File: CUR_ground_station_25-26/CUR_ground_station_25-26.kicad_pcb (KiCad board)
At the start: 4 copper layers, 73.9 x 53.3 mm, 81 parts, among them J1 Conn_01x02, J2 UJ20-C-H-G-SMT-P16-TR, J3 Conn_Coaxial_Small, J4 Conn_01x04_Pin, Q1 NTR4003N, Q2 NTR4003N, SW1 PTS815SJM250SMTRLFS, SW2 PTS815SJM250SMTRLFS, SW3 PTS815SJM250SMTRLFS, SW4 PTS815SJM250SMTRLFS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

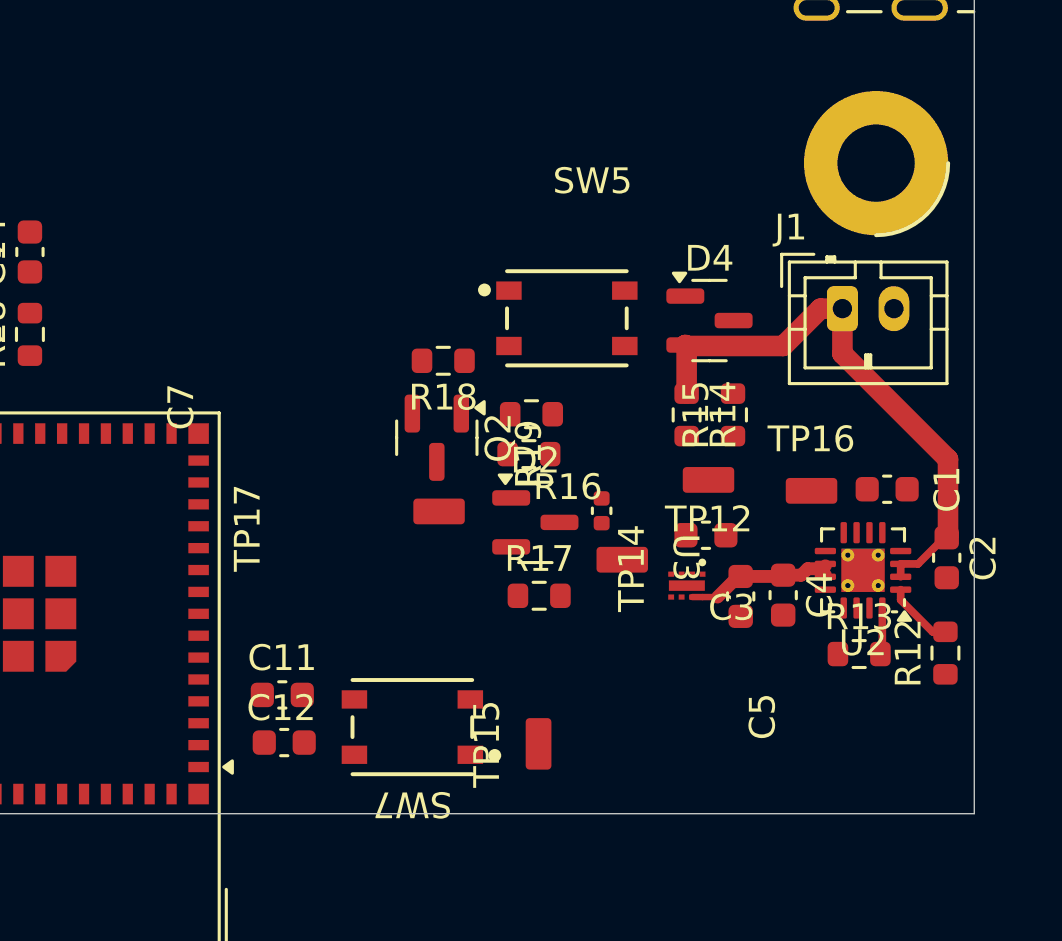
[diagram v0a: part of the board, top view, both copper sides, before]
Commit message: more power layout ing
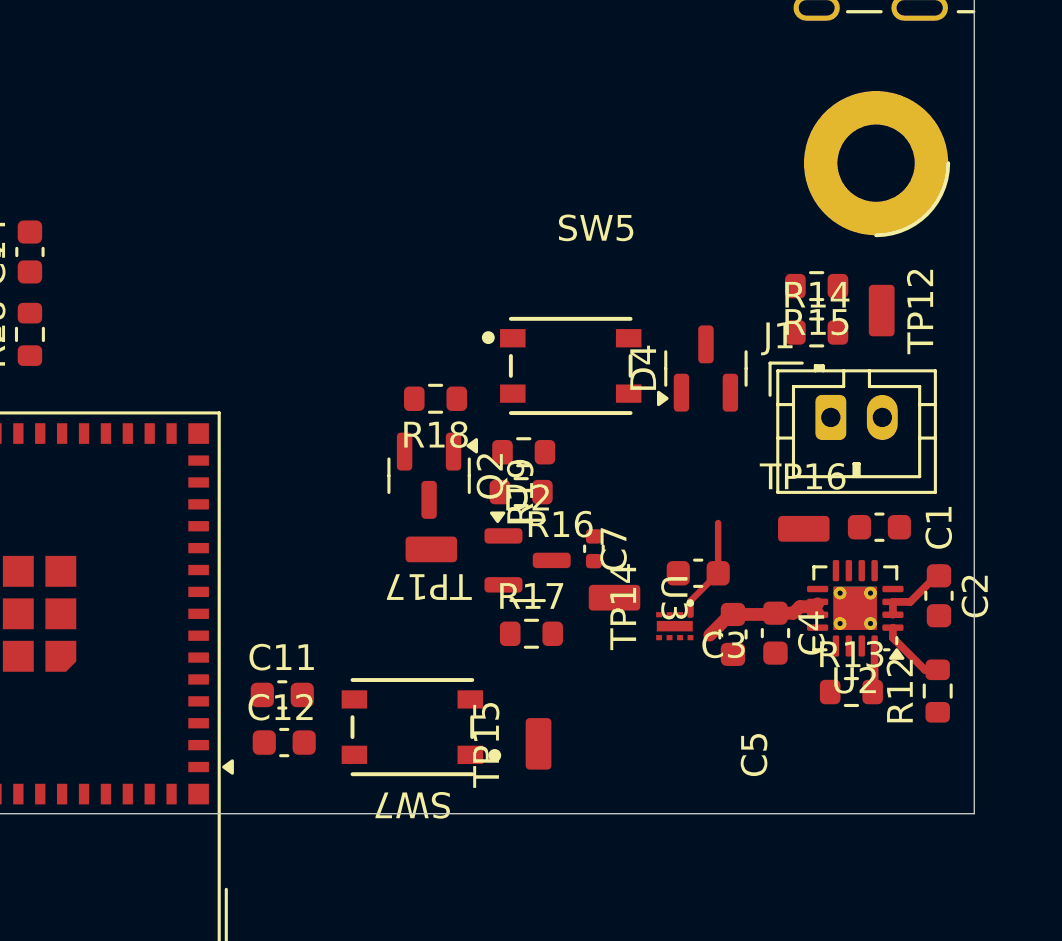
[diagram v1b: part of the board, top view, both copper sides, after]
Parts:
- moved TP12 9.41 mm to (118.8, 83.8), turned to -90 degrees
- moved R14 5.98 mm to (116.3, 84.6), turned to 0 degrees
- moved R15 5.96 mm to (116.3, 82.8), turned to 180 degrees
- moved J1 4.25 mm to (116.8, 87.9)
- moved D4 1.87 mm to (112.0, 86.0), turned to 90 degrees
- moved SW5 1.86 mm to (106.7, 85.9)
- moved U3 1.64 mm to (110.7, 96.0)
- moved C5 1.51 mm to (111.6, 94.0)
- moved R18 1.51 mm to (101.5, 87.2)
- moved TP17 1.51 mm to (101.3, 93.1)
- moved R12 1.51 mm to (121.0, 98.6)
- moved R17 1.51 mm to (105.2, 96.3)
- moved TP16 1.51 mm to (115.8, 92.2)
- moved TP14 1.51 mm to (108.4, 94.9)
- moved C7 1.51 mm to (107.6, 93.0)
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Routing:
- net +BATT: track 21.9 -> 2.78 mm
- net +3V3: track 0.00 -> 4.01 mm
- net IN: track 5.97 -> 4.98 mm

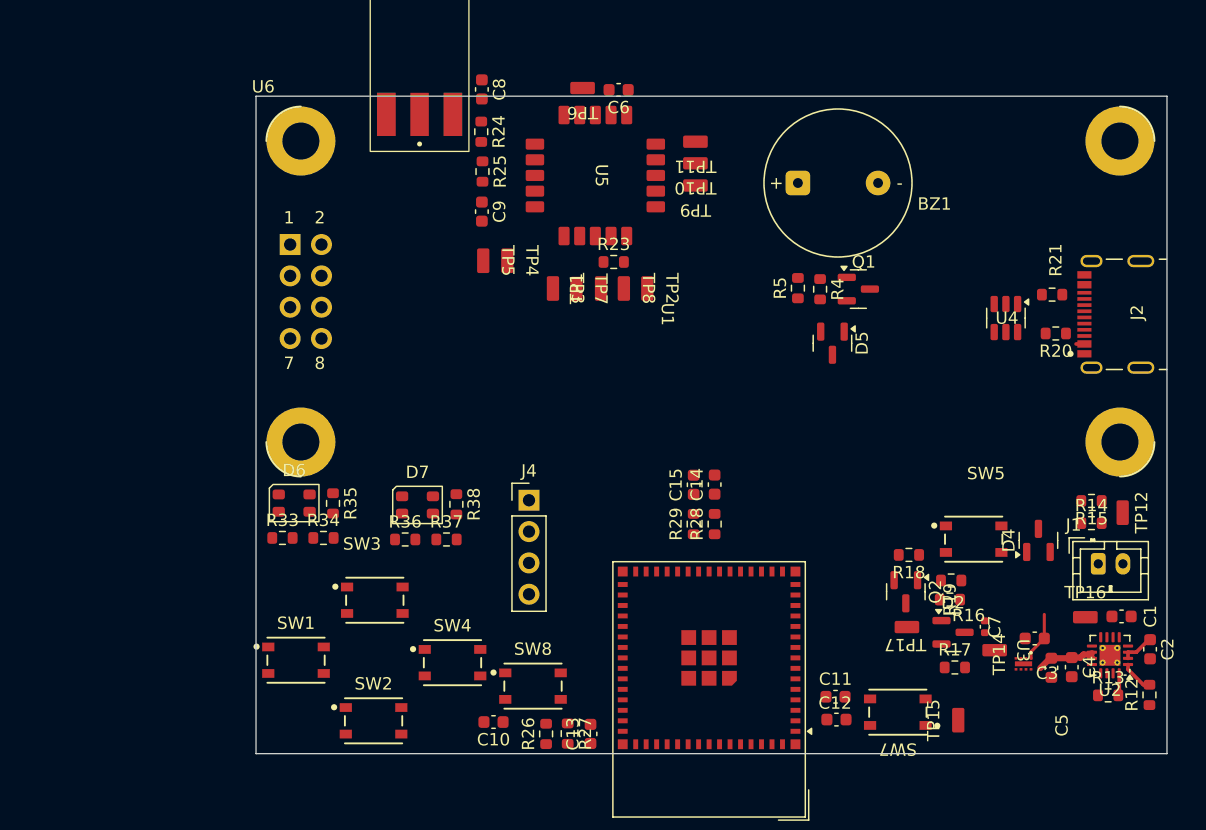
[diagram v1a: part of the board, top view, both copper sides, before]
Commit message: Update board shape, display, and USB C placement
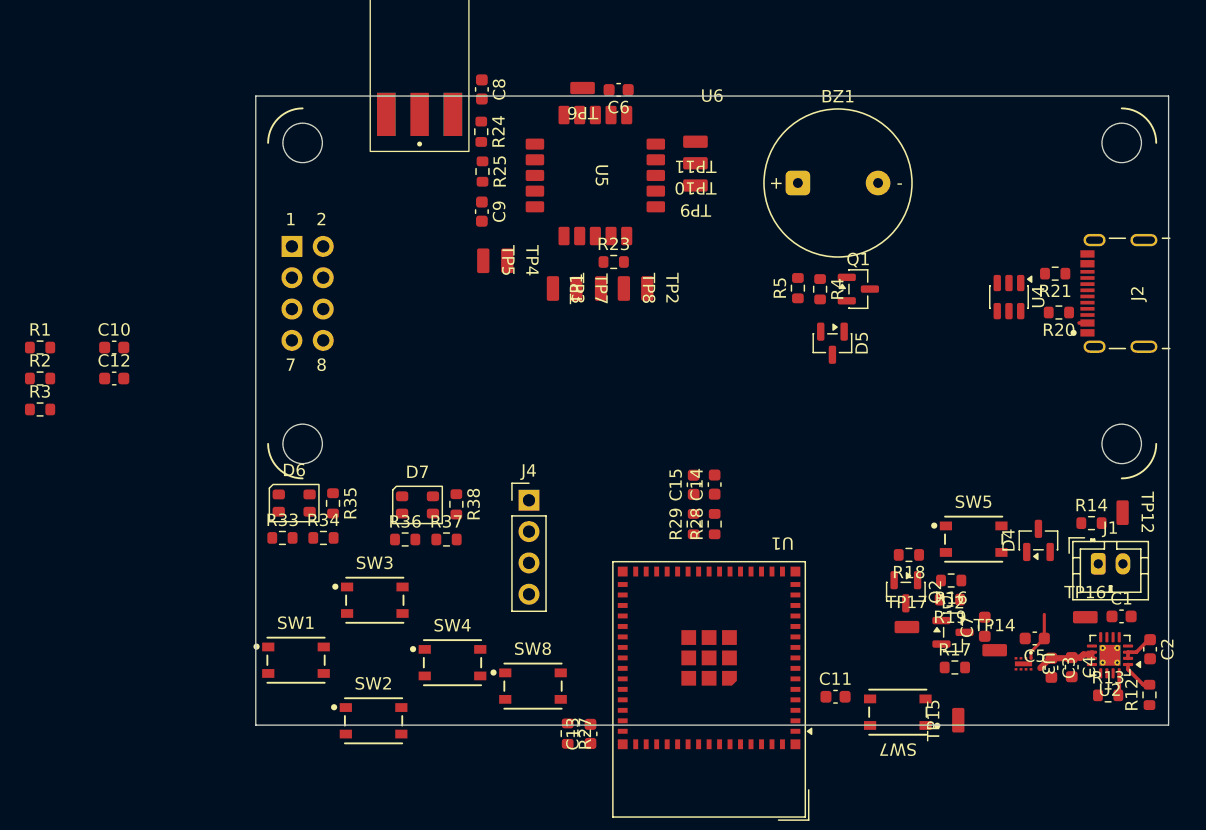
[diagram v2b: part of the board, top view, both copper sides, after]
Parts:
- removed R15: 35k, Resistor_SMD:R_0603_1608Metric
- removed R26: 0, Resistor_SMD:R_0603_1608Metric
- added R1: 10k, Resistor_SMD:R_0603_1608Metric, F.Cu at (31.0, 70.4)
- added R2: 10k, Resistor_SMD:R_0603_1608Metric, F.Cu at (31.0, 72.9)
- added R3: 10k, Resistor_SMD:R_0603_1608Metric, F.Cu at (31.0, 75.4)
- C10: value 100n -> 10u
- C11: value 100n -> 1u
- C12: value 22u -> 10u
- C7: value 1u -> 10u; footprint Capacitor_SMD:C_0402_1005Metric -> Capacitor_SMD:C_0603_1608Metric
- R13: value RC0603FR-071K74L -> 1.74k
- R16, R17: value 300 -> 270
- R18, R19: value 100k -> 10k
- R5: value 150 -> 270
- moved C12 64.8 mm to (37.0, 72.9)
- moved C10 43.2 mm to (37.0, 70.4), turned to 0 degrees
- moved J2 1.72 mm to (120.5, 66.0)
- moved R20 1.72 mm to (113.6, 67.6)
- moved R21 1.72 mm to (113.3, 64.4)
- moved U4 1.72 mm to (109.6, 66.3)
- moved U6 0.21 mm to (49.5, 51.0)
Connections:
- C10 pad 1: Net-(C10-Pad1) -> +3V3
- SW8 pad 2: Net-(C10-Pad1) -> /MCU/EN
- U5 pad 17: (no net) -> unconnected-(U5-NC-Pad17)
- U5 pad 4: (no net) -> unconnected-(U5-NC-Pad4)
- U5 pad 5: (no net) -> unconnected-(U5-NC-Pad5)
- U5 pad 8: (no net) -> unconnected-(U5-NC-Pad8)
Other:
- board size 73.9 x 53.3 mm -> 74 x 51 mm

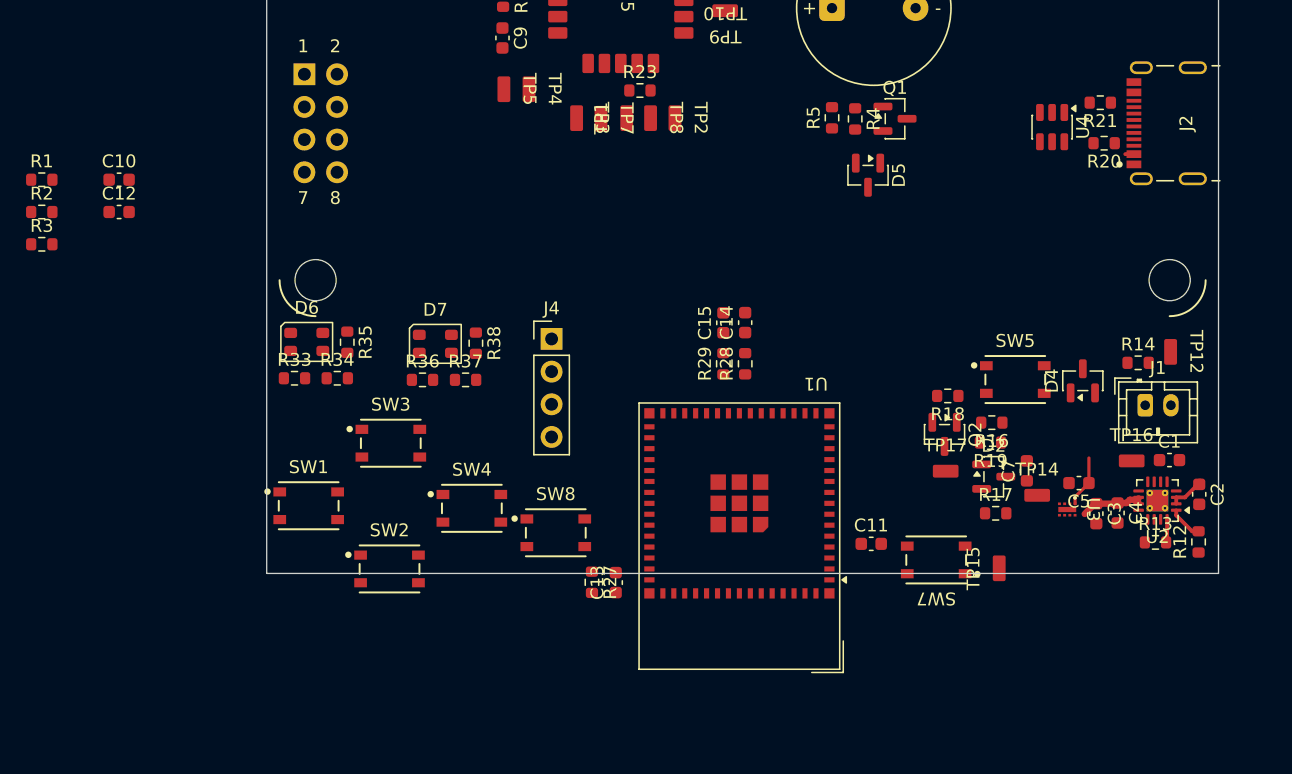
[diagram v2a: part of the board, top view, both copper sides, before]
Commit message: Fix USB capacitors
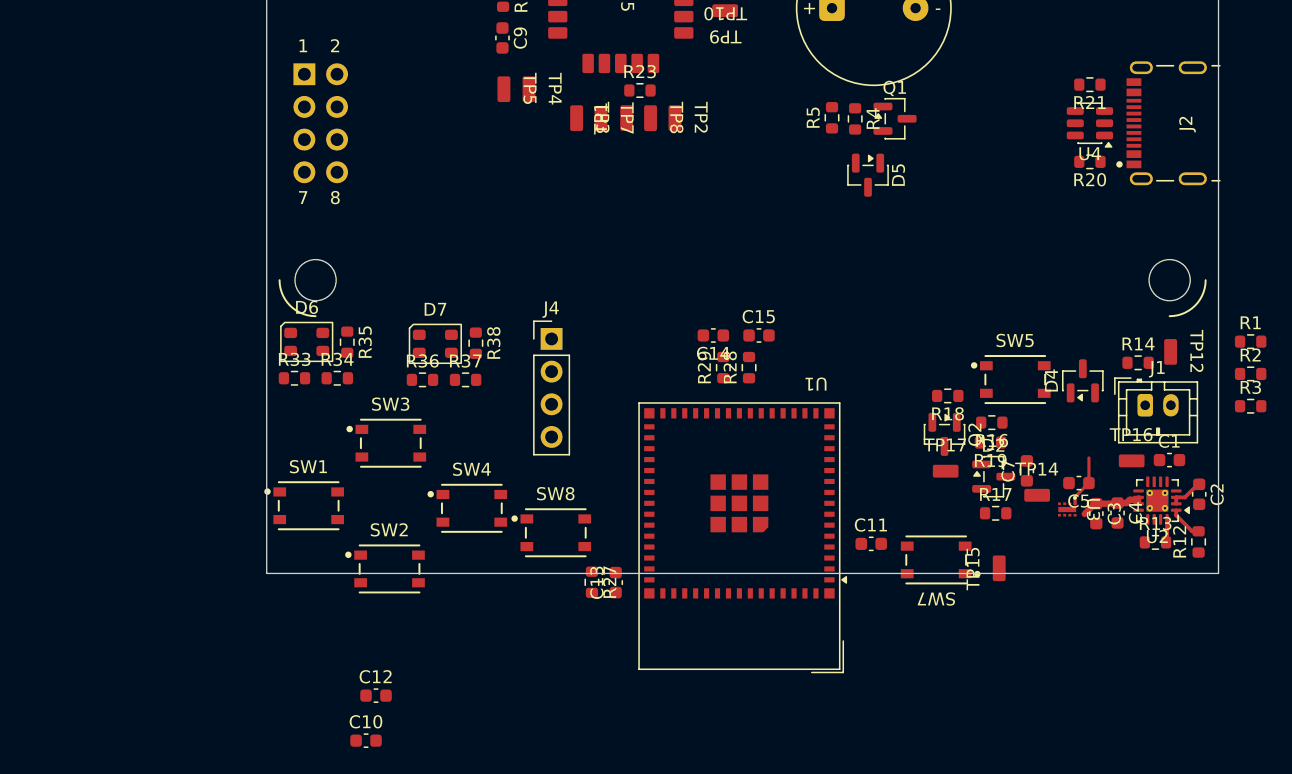
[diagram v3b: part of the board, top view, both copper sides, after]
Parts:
- moved R1 94.8 mm to (125.0, 83.0)
- moved R2 94.8 mm to (125.0, 85.5)
- moved R3 94.8 mm to (125.0, 88.0)
- moved C10 47.6 mm to (56.2, 114.0)
- moved C12 42.6 mm to (57.0, 110.5)
- moved U4 2.95 mm to (112.5, 66.0), turned to 180 degrees
- moved C15 2.94 mm to (86.8, 82.5), turned to 0 degrees
- moved C14 2.67 mm to (83.2, 82.5), turned to 180 degrees
- moved R20 1.82 mm to (112.5, 69.0)
- moved R21 1.62 mm to (112.5, 63.0)
- moved R28 0.42 mm to (86.0, 85.0)
- moved R29 0.30 mm to (84.0, 85.0)
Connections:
- C15 pad 1: /MCU/USB_D+ -> /MCU/USB_D-
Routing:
- net VBUS: track 0.67 -> 0.00 mm
